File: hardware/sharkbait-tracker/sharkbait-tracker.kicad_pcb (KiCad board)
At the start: 2 copper layers, 3 parts, among them U1 LLCC68, U2 STM32L031G6Ux, Y1 32MHz

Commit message: Most of the layout done, but might break things
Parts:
- added BT1: LiPo, Connector_PinHeader_2.00mm:PinHeader_1x02_P2.00mm_Vertical, F.Cu at (126.5, 83.8)
- added C1: 0.1uF, Capacitor_SMD:C_0402_1005Metric, F.Cu at (107.7, 72.1)
- added C10: 6.8p, Capacitor_SMD:C_0402_1005Metric, F.Cu at (133.1, 77.4)
- added C11: 0.1uF, Capacitor_SMD:C_0402_1005Metric, F.Cu at (133.6, 72.9)
- added C12: 6.8p, Capacitor_SMD:C_0402_1005Metric, F.Cu at (134.6, 75.9)
- added C13: 4.7p, Capacitor_SMD:C_0402_1005Metric, F.Cu at (136.1, 77.5)
- added C14: 0, Capacitor_SMD:C_0402_1005Metric, F.Cu at (138.2, 77.5)
- added C15: 3.3p, Capacitor_SMD:C_0402_1005Metric, F.Cu at (137.2, 77.5)
- added C16: 68p, Capacitor_SMD:C_0402_1005Metric, F.Cu at (136.1, 75.4)
- added C17: 0.1uF, Capacitor_SMD:C_0402_1005Metric, F.Cu at (136.0, 80.5)
- added C18: 0.1uF, Capacitor_SMD:C_0402_1005Metric, F.Cu at (136.0, 82.8)
- added C19: 0, Capacitor_SMD:C_0402_1005Metric, F.Cu at (139.4, 77.5)
- added C2: 10uF, Capacitor_SMD:C_0603_1608Metric, F.Cu at (122.9, 76.0)
- added C3: 1uF, Capacitor_SMD:C_0402_1005Metric, F.Cu at (125.8, 75.2)
- added C4: 10uF, Capacitor_SMD:C_0603_1608Metric, F.Cu at (124.5, 76.0)
- added C5: 0.1uF, Capacitor_SMD:C_0402_1005Metric, F.Cu at (125.8, 77.1)
- added C6: 1uF, Capacitor_SMD:C_0402_1005Metric, F.Cu at (129.7, 72.2)
- added C7: 0.1uF, Capacitor_SMD:C_0402_1005Metric, F.Cu at (128.4, 79.2)
- added C8: 0.1uF, Capacitor_SMD:C_0402_1005Metric, F.Cu at (129.6, 81.1)
- added C9: 68p, Capacitor_SMD:C_0402_1005Metric, F.Cu at (132.6, 72.9)
- added D1: RED, LED_SMD:LED_0603_1608Metric, F.Cu at (142.9, 82.6)
- added H1: MountingHole, MountingHole:MountingHole_2.2mm_M2, F.Cu at (120.0, 73.3)
- added H2: MountingHole, MountingHole:MountingHole_2.2mm_M2, F.Cu at (139.1, 83.4)
- added J1: Conn_01x04, Connector_Molex:Molex_PicoBlade_53047-0410_1x04_P1.25mm_Vertical, F.Cu at (122.8, 82.8)
- added J2: Conn_Coaxial_Small, Connector_Coaxial:SMA_Samtec_SMA-J-P-H-ST-EM1_EdgeMount, F.Cu at (142.7, 77.0)
- added JP1: RST, Jumper:SolderJumper-2_P1.3mm_Open_RoundedPad1.0x1.5mm, B.Cu at (135.4, 80.2)
- added JP2: BOOT, Jumper:SolderJumper-2_P1.3mm_Open_RoundedPad1.0x1.5mm, B.Cu at (135.4, 83.6)
- added JP3: Ublox_VCCIO, Jumper:SolderJumper-2_P1.3mm_Open_TrianglePad1.0x1.5mm, B.Cu at (114.7, 74.0)
- added L1: 68u, Inductor_SMD:L_0603_1608Metric, F.Cu at (133.3, 74.7)
- added L2: 4.7n, Inductor_SMD:L_0402_1005Metric, F.Cu at (132.6, 75.9)
- added L3: 3.9n, Inductor_SMD:L_0402_1005Metric, F.Cu at (134.6, 77.0)
- added L4: 10n, Inductor_SMD:L_0402_1005Metric, F.Cu at (137.2, 75.4)
- added L5: 0R, Inductor_SMD:L_0402_1005Metric, F.Cu at (138.7, 75.9)
- added R1: 4.7k, Resistor_SMD:R_0402_1005Metric, F.Cu at (109.9, 72.1)
- added R10: 220, Resistor_SMD:R_0402_1005Metric, F.Cu at (119.6, 76.5)
- added R11: 220, Resistor_SMD:R_0402_1005Metric, F.Cu at (119.6, 80.3)
- added R12: 4.7k, Resistor_SMD:R_0402_1005Metric, F.Cu at (131.8, 84.6)
- added R2: 4.7k, Resistor_SMD:R_0402_1005Metric, F.Cu at (113.5, 72.1)
- added R3: 220, Resistor_SMD:R_0402_1005Metric, F.Cu at (119.6, 79.0)
- added R4: 220, Resistor_SMD:R_0402_1005Metric, F.Cu at (119.6, 77.7)
- added R7: 4.7k, Resistor_SMD:R_0402_1005Metric, F.Cu at (135.3, 84.5)
- added R8: 4.7k, Resistor_SMD:R_0402_1005Metric, F.Cu at (137.2, 80.5)
- added R9: 75, Resistor_SMD:R_0402_1005Metric, F.Cu at (138.7, 80.0)
- added TP1: DBG_RX, TestPoint:TestPoint_Pad_D1.0mm, B.Cu at (132.7, 82.9)
- added TP2: DBG_TX, TestPoint:TestPoint_Pad_D1.0mm, B.Cu at (132.7, 80.7)
- added U2: XC6206PxxxMR, Package_TO_SOT_SMD:SOT-23-3, F.Cu at (122.9, 79.3)
- added U3: XT25F32FDTIGT, Package_SON:Winbond_USON-8-1EP_3x2mm_P0.5mm_EP0.2x1.6mm, F.Cu at (126.6, 80.2)
- added U4: LLCC68, Package_DFN_QFN:QFN-24-1EP_4x4mm_P0.5mm_EP2.7x2.7mm, F.Cu at (129.0, 75.4)
- U1: value LLCC68 -> Quectel_L96; footprint Package_DFN_QFN:QFN-24-1EP_4x4mm_P0.5mm_EP2.7x2.7mm -> RF_Module_Custom:CAM-M8_QuectelL96
- moved U5 24.9 mm to (132.8, 81.3), turned to 180 degrees
- moved Y1 23.1 mm to (125.0, 72.9)
- moved U1 4.31 mm to (103.0, 78.7), turned to 90 degrees
- renumbered U2 to U5
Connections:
- U1 pad 1: +3.3V -> /UBLOX_VCCIO
- U1 pad 10: +3.3V -> GND
- U1 pad 11: +3.3V -> GND
- U1 pad 12: unconnected-(U1-DIO2-Pad12) -> GND
- U1 pad 13: unconnected-(U1-DIO1-Pad13) -> GND
- U1 pad 14: unconnected-(U1-BUSY-Pad14) -> GND
- U1 pad 15: unconnected-(U1-NRESET-Pad15) -> GND
- U1 pad 16: unconnected-(U1-MISO-Pad16) -> Net-(U1-RF_IN)
- U1 pad 17: unconnected-(U1-MOSI-Pad17) -> Net-(U1-RF_IN)
- U1 pad 18: unconnected-(U1-SCK-Pad18) -> GND
- U1 pad 19: unconnected-(U1-NSS-Pad19) -> GND
- U1 pad 2: GND -> unconnected-(U1-3D_FIX-Pad2)
- U1 pad 20: GND -> unconnected-(U1-JAM_IND-Pad20)
- U1 pad 21: Net-(U1-RFI_N) -> GND
- U1 pad 22: Net-(U1-RFI_N) -> GND
- U1 pad 23: unconnected-(U1-RFO-Pad23) -> /R_nRST
- U1 pad 25: GND -> /GPS_TX
- U1 pad 3: /RF_XTA -> /SDA_NC
- U1 pad 4: /RF_XTB -> GND
- U1 pad 6: unconnected-(U1-DIO3-Pad6) -> /SCL_NC
- U1 pad 8: GND -> +3.3V
- U1 pad 9: unconnected-(U1-DCC_SW-Pad9) -> +3.3V
- U5 pad 10: unconnected-(U2-PA4-Pad10) -> /RF_CS
- U5 pad 11: unconnected-(U2-PA5-Pad11) -> /SCK
- U5 pad 12: unconnected-(U2-PA6-Pad12) -> /MISO
- U5 pad 13: unconnected-(U2-PA7-Pad13) -> /MOSI
- U5 pad 14: unconnected-(U2-PB0-Pad14) -> /RF_nRST
- U5 pad 15: unconnected-(U2-PB1-Pad15) -> /RF_BUSY
- U5 pad 18: unconnected-(U2-PA8-Pad18) -> /GPS_nRST
- U5 pad 19: unconnected-(U2-PA9-Pad19) -> /DBG_TX
- U5 pad 20: unconnected-(U2-PA10-Pad20) -> /DBG_RX
- U5 pad 21: unconnected-(U2-PA13-Pad21) -> /SWDIO
- U5 pad 22: unconnected-(U2-PA14-Pad22) -> /SWCLK
- U5 pad 23: unconnected-(U2-PA15-Pad23) -> /FLASH_CS
- U5 pad 24: unconnected-(U2-PB3-Pad24) -> /OWI
- U5 pad 27: unconnected-(U2-BOOT0-Pad27) -> /BOOT
- U5 pad 3: unconnected-(U2-PC15-Pad3) -> /LED
- U5 pad 4: unconnected-(U2-NRST-Pad4) -> /NRST
- U5 pad 6: unconnected-(U2-PA0-Pad6) -> /GPS_1PPS
- U5 pad 8: unconnected-(U2-PA2-Pad8) -> /TX
- U5 pad 9: unconnected-(U2-PA3-Pad9) -> /RX
- Y1 pad 1: /RF_XTA -> /RF Transmitter/RF_XTA
- Y1 pad 3: /RF_XTB -> /RF Transmitter/RF_XTB
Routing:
- net +3.3V: track 0.00 -> 26.9 mm, vias 0 -> 11
- net /GPS_nRST: track 0.00 -> 12.7 mm
- net /OWI: track 0.00 -> 12.7 mm, vias 0 -> 1
- net /FLASH_CS: track 0.00 -> 12.7 mm, vias 0 -> 2
- net /SWCLK: track 0.00 -> 12.1 mm
- net /SCK: track 0.00 -> 12.0 mm, vias 0 -> 2
- net /R_nRST: track 0.00 -> 10.8 mm
- net /SWDIO: track 0.00 -> 10.3 mm
- net /MOSI: track 0.00 -> 9.53 mm, vias 0 -> 2
- net /GPS_TX: track 0.00 -> 9.36 mm
- net /MISO: track 0.00 -> 9.29 mm, vias 0 -> 3
- net +BATT: track 0.00 -> 8.96 mm, vias 0 -> 2
- net /GPS_RX: track 0.00 -> 6.97 mm
- net GND: track 0.00 -> 4.93 mm, vias 0 -> 1
- net /NRST: track 0.00 -> 4.87 mm, vias 0 -> 1
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- added copper zone on B.Cu, net +3.3V
- added copper zone on F.Cu, net GND
- added copper zone on In1.Cu, net GND
- added copper zone on In2.Cu, net GND
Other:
- board outline added: 41.8 x 14 mm
- copper layers 2 -> 4
- board text added: "RST BOOT"
- board text added: "TX RX"

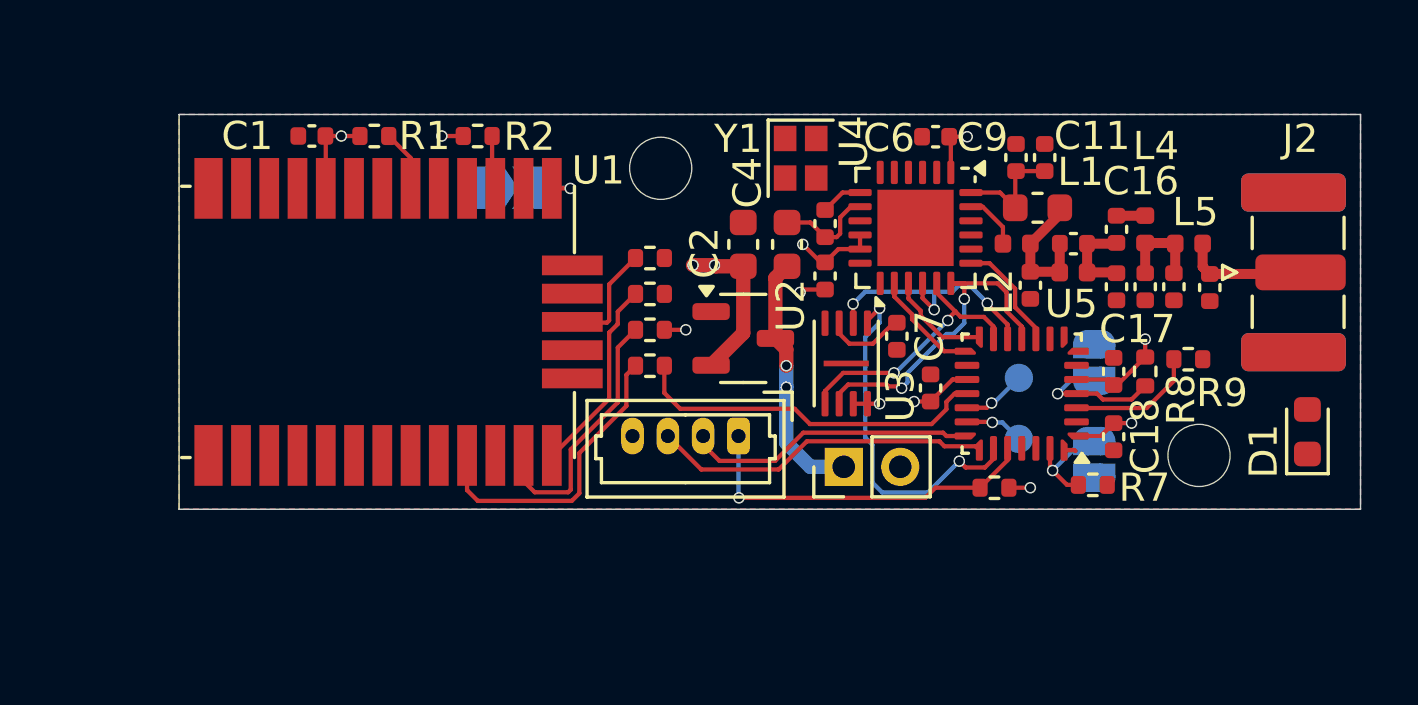
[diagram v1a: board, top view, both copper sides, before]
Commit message: Everything fits, might rearrange a little
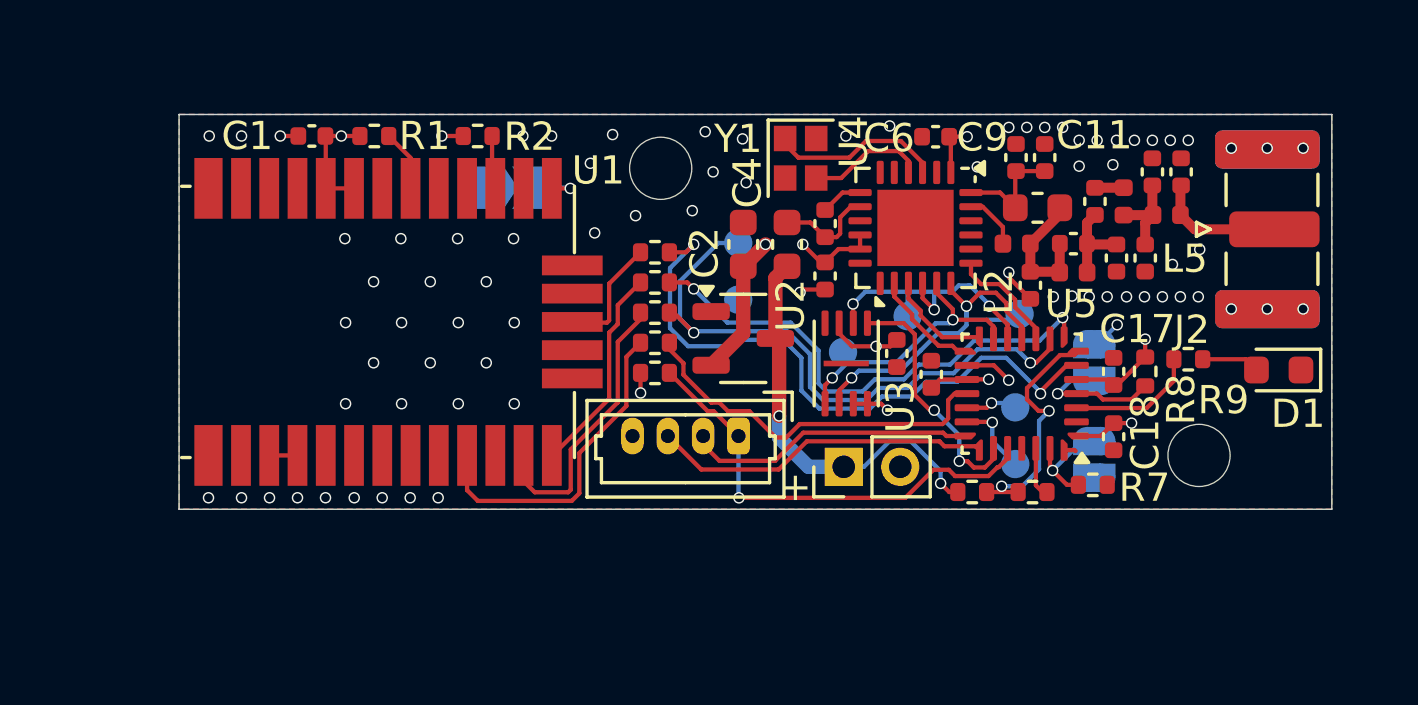
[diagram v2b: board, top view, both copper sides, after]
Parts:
- added R13: 27k, Resistor_SMD:R_0402_1005Metric, F.Cu at (133.2, 84.7)
- added R5: 100k, Resistor_SMD:R_0402_1005Metric, F.Cu at (131.0, 84.7)
- added TP3: SCK, TestPoint:TestPoint_Pad_D1.0mm, B.Cu at (132.7, 78.4)
- added TP4: MISO, TestPoint:TestPoint_Pad_D1.0mm, B.Cu at (128.8, 78.5)
- added TP5: MOSI, TestPoint:TestPoint_Pad_D1.0mm, B.Cu at (126.5, 79.8)
- added TP6: GPS_TX, TestPoint:TestPoint_Pad_D1.0mm, B.Cu at (122.8, 77.9)
- added TP7: GPS_RX, TestPoint:TestPoint_Pad_D1.0mm, B.Cu at (122.8, 75.9)
- moved R12 12.7 mm to (119.8, 80.5), turned to 0 degrees
- moved C19 4.22 mm to (138.4, 73.4), turned to 90 degrees
- moved C14 4.13 mm to (137.4, 73.4), turned to 90 degrees
- moved D1 2.41 mm to (141.9, 80.4), turned to 180 degrees
- moved J2 1.78 mm to (141.7, 75.4)
- moved L5 1.28 mm to (137.9, 74.9)
- moved C16 1.25 mm to (135.4, 74.5)
- moved L4 1.25 mm to (136.4, 74.5)
- moved TP2 1.05 mm to (132.6, 81.7)
- moved C13 1.02 mm to (136.1, 76.5)
- moved C15 1.02 mm to (137.2, 76.5)
- moved TP1 0.90 mm to (132.6, 83.7)
- moved R11 0.83 mm to (119.8, 79.5)
- moved R3 0.64 mm to (119.8, 78.4)
- moved C7 0.61 mm to (128.4, 79.8)
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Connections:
- U5 pad 26: unconnected-(U5-PB7-Pad26) -> /UVP_DRV
- U5 pad 7: unconnected-(U5-PA1-Pad7) -> /UVP_SENS
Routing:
- net /GPS_1PPS: track 0.00 -> 22.5 mm, vias 0 -> 2
- net /RX: track 0.76 -> 21.6 mm, vias 1 -> 2
- net /TX: track 0.00 -> 18.8 mm, vias 0 -> 2
- net /UVP_SENS: track 0.00 -> 8.60 mm, vias 0 -> 2
- net /RF Transmitter/RF_XTA: track 0.00 -> 6.17 mm
- net +BATT: track 8.96 -> 14.4 mm
- net GND: track 4.93 -> 9.61 mm, vias 1 -> 78
- net /RF Transmitter/RF_XTB: track 0.00 -> 4.21 mm
- net /FLASH_CS: track 12.7 -> 8.96 mm
- net /OWI: track 12.7 -> 16.2 mm
- net Net-(D1-A): track 0.00 -> 2.06 mm
- net /UVP_DRV: track 0.00 -> 1.80 mm
- net /SCK: track 12.0 -> 13.3 mm
- net Net-(U1-RF_IN): track 0.00 -> 1.00 mm
- net /R_nRST: track 10.8 -> 11.7 mm
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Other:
- board size 41.8 x 14 mm -> 40.8 x 14 mm
- board text added: "+"
- board text added: "<uBlox"
- board text added: "MISO"
- board text added: "MOSI"
- board text added: "SCK"
- board text added: "^G"
- board text added: "by bry >:3"
- board text added: "gRX gTX"

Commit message: Removed battery voltage divider again, and rounded corners
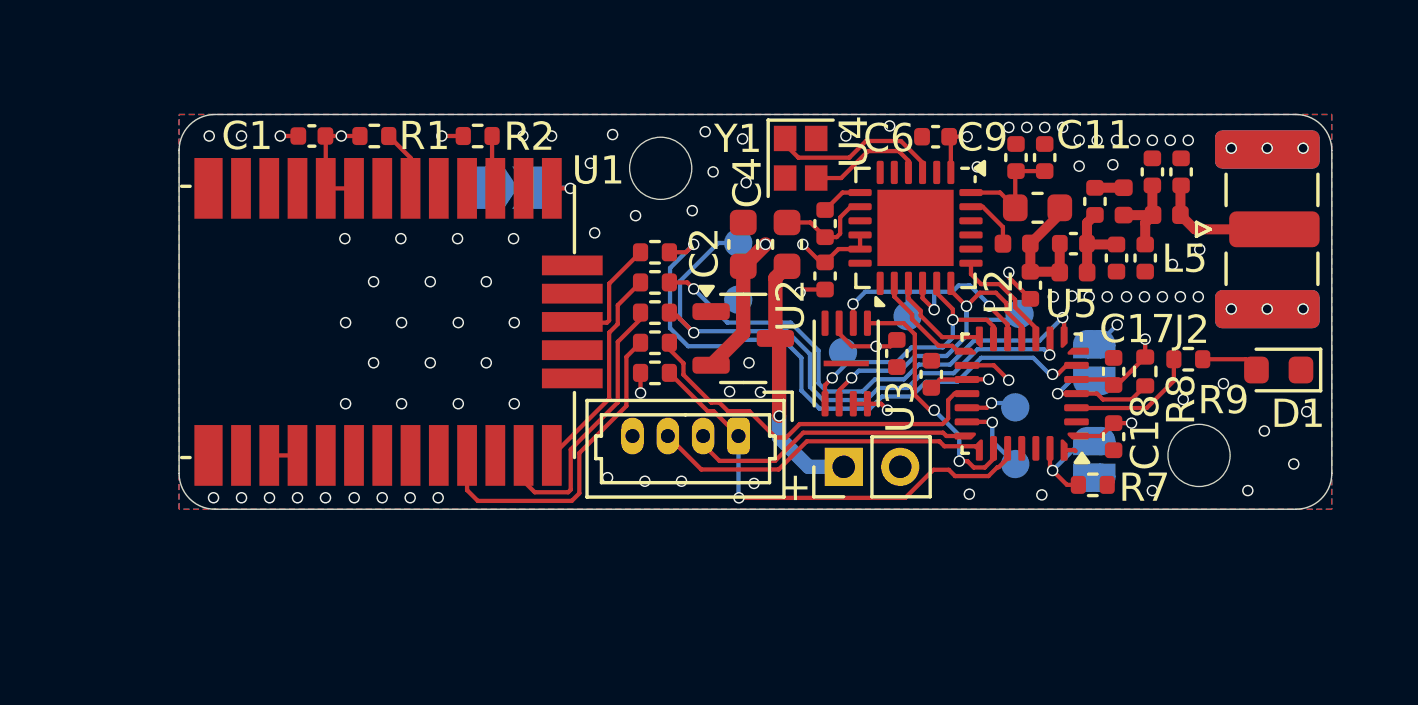
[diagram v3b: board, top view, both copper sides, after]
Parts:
- removed R13: 27k, Resistor_SMD:R_0402_1005Metric
- removed R5: 100k, Resistor_SMD:R_0402_1005Metric
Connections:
- U5 pad 26: /UVP_DRV -> unconnected-(U5-PB7-Pad26)
- U5 pad 7: /UVP_SENS -> unconnected-(U5-PA1-Pad7)
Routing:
- net /UVP_SENS: track 8.60 -> 0.00 mm, vias 2 -> 0
- net +BATT: track 14.4 -> 9.00 mm, vias 2 -> 1
- net /UVP_DRV: track 1.80 -> 0.00 mm
- net /GPS_1PPS: track 22.5 -> 21.8 mm
- net GND: vias 78 -> 94
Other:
- outline, holes or cut-outs redrawn
- board text added: "ANT"
- board text added: "Sharkbait miniature GPS tracker"
- board text added: "v1.0"

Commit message: Combination antenna footprint and build automation
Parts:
- J2: footprint Connector_Coaxial:SMA_Samtec_SMA-J-P-H-ST-EM1_EdgeMount -> Connector_Coaxial_Custom:SMA_Samtec_SMA-J-P-H-ST-EM1_EdgeMount_WireWhip
- U4: footprint Package_DFN_QFN:QFN-24-1EP_4x4mm_P0.5mm_EP2.7x2.7mm -> Package_DFN_QFN:QFN-24-1EP_4x4mm_P0.5mm_EP2.7x2.7mm_ThermalVias
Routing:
- net GND: vias 94 -> 103
